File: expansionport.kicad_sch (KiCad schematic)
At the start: 18 parts, among them J20 C64_Expansion_Port, U31 74LS04, U32 74LVC374, U33 74LVC374, U34 74LVC374, U35 74LS374, U36 74LS374, U37 74LS374, U38 74LVC374, U39 74LVC374, U40 74LS374, U41 74LS374, U42 74LS06

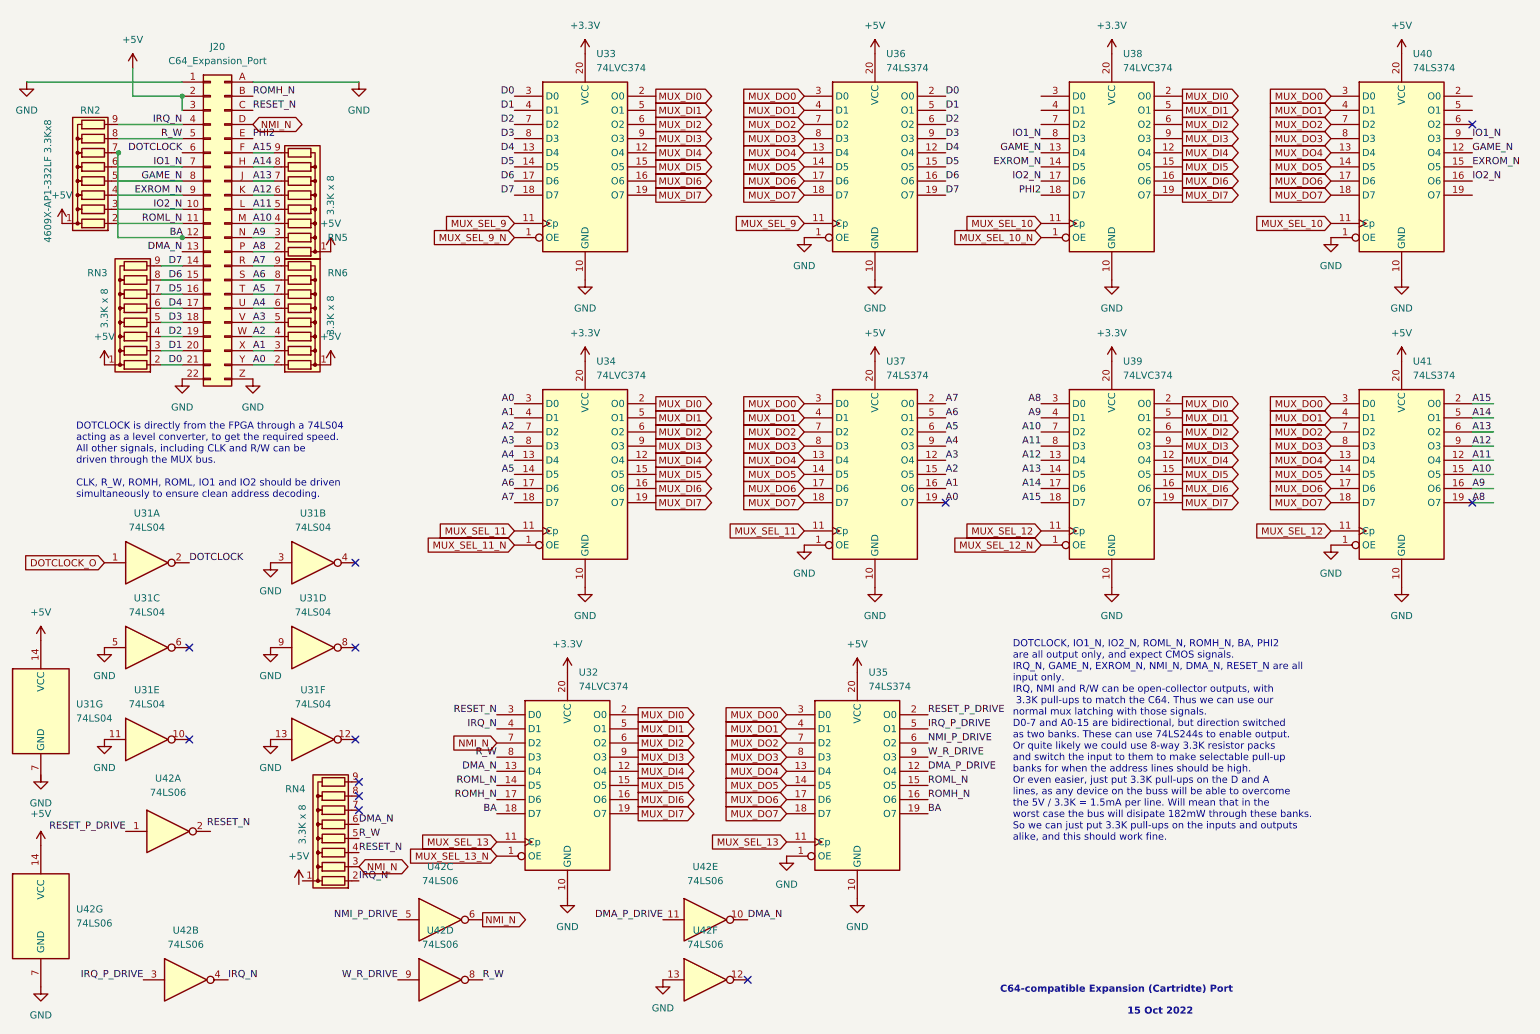
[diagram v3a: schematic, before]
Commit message: route part of cart port
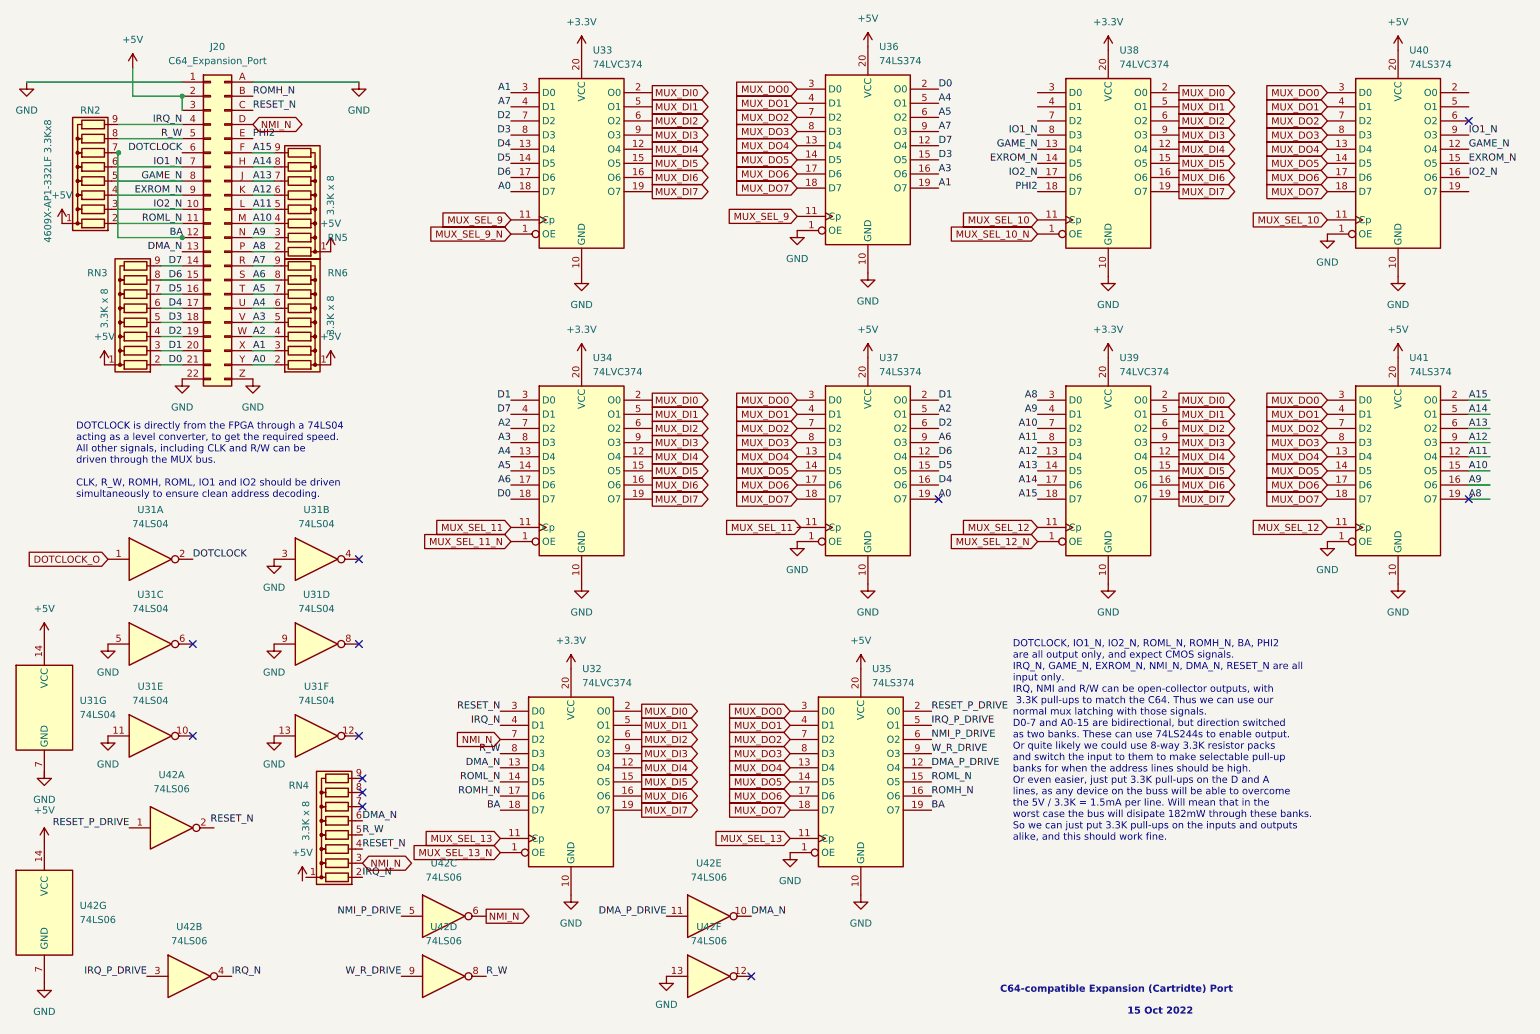
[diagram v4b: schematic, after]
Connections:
- net A0: now also U33.18 (D7); no longer U34.3 (D0)
- net A1: now also U33.3 (D0), U36.19 (O7); no longer U34.4 (D1), U37.16 (O6)
- net A2: now also U37.5 (O1); no longer U37.15 (O5)
- net A3: now also U36.16 (O6); no longer U37.12 (O4)
- net A4: now also U36.5 (O1); no longer U37.9 (O3)
- net A5: now also U36.6 (O2); no longer U37.6 (O2)
- net A6: now also U37.9 (O3); no longer U37.5 (O1)
- net A7: now also U33.4 (D1), U36.9 (O3); no longer U34.18 (D7), U37.2 (O0)
- net D0: now also U34.18 (D7); no longer U33.3 (D0)
- net D1: now also U34.3 (D0), U37.2 (O0); no longer U33.4 (D1), U36.5 (O1)
- net D2: now also U37.6 (O2); no longer U36.6 (O2)
- net D3: now also U36.15 (O5); no longer U36.9 (O3)
- net D4: now also U37.16 (O6); no longer U36.12 (O4)
- net D5: now also U37.15 (O5); no longer U36.15 (O5)
- net D6: now also U37.12 (O4); no longer U36.16 (O6)
- net D7: now also U34.4 (D1), U36.12 (O4); no longer U33.18 (D7), U36.19 (O7)
- net MUX_SEL_11: no longer U37.11 (Cp)
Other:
- moved on the sheet: RN4, U31A, U31B, U31C, U31D, U31E, U31F, U31G, U32, U33, U34, U35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

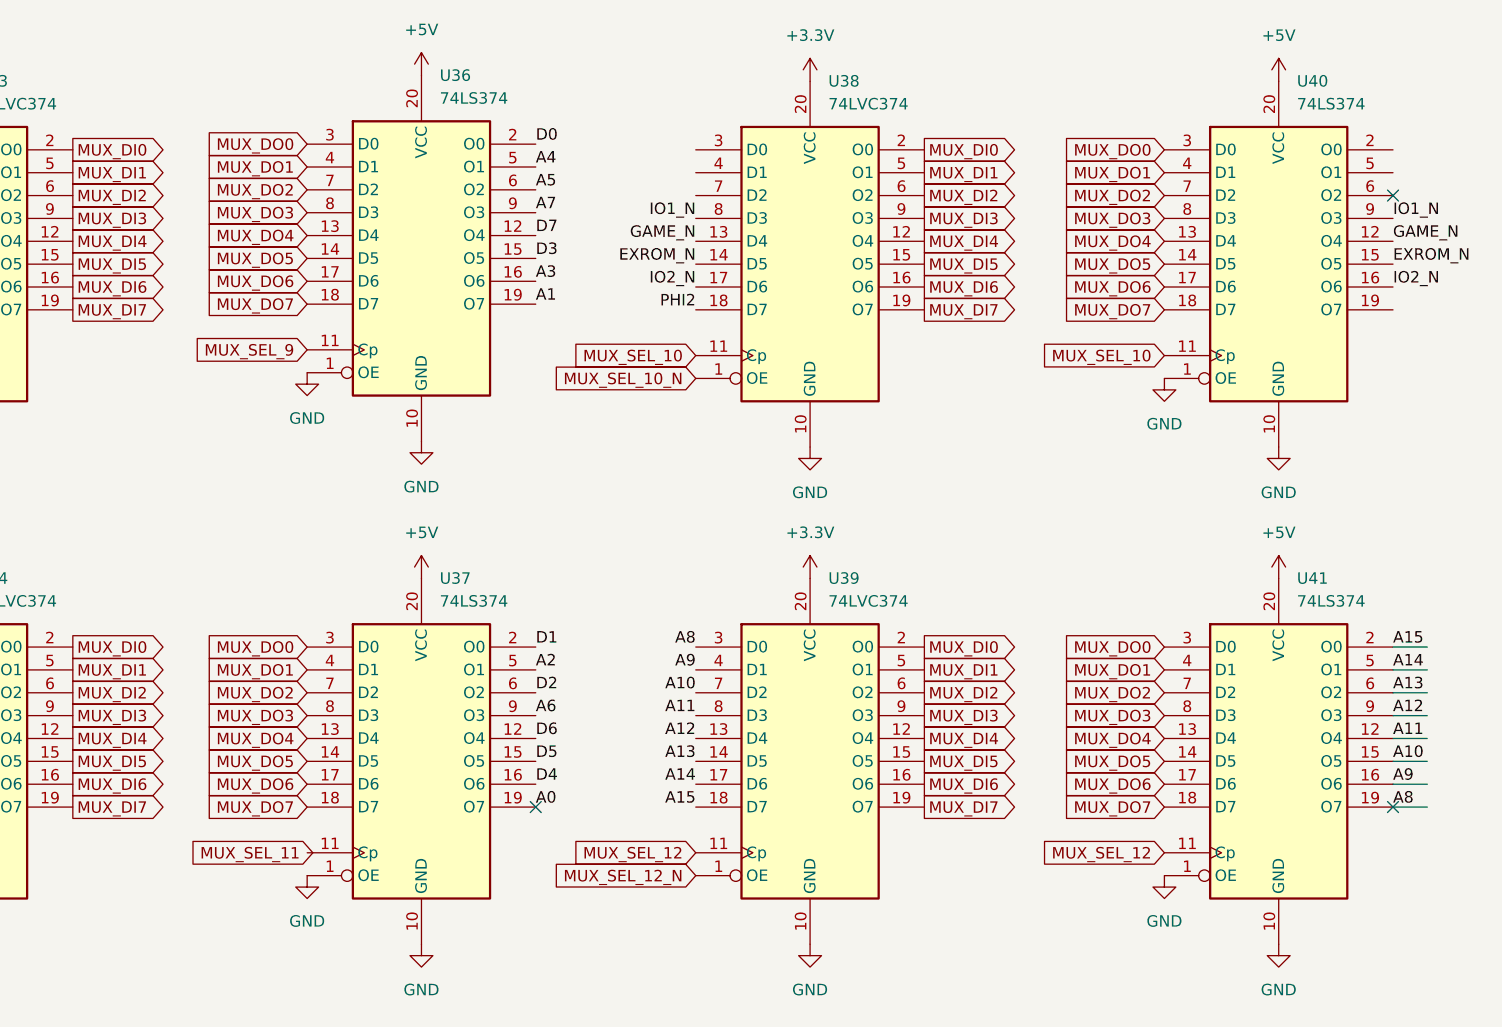
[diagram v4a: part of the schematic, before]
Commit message: begin routing mux bus
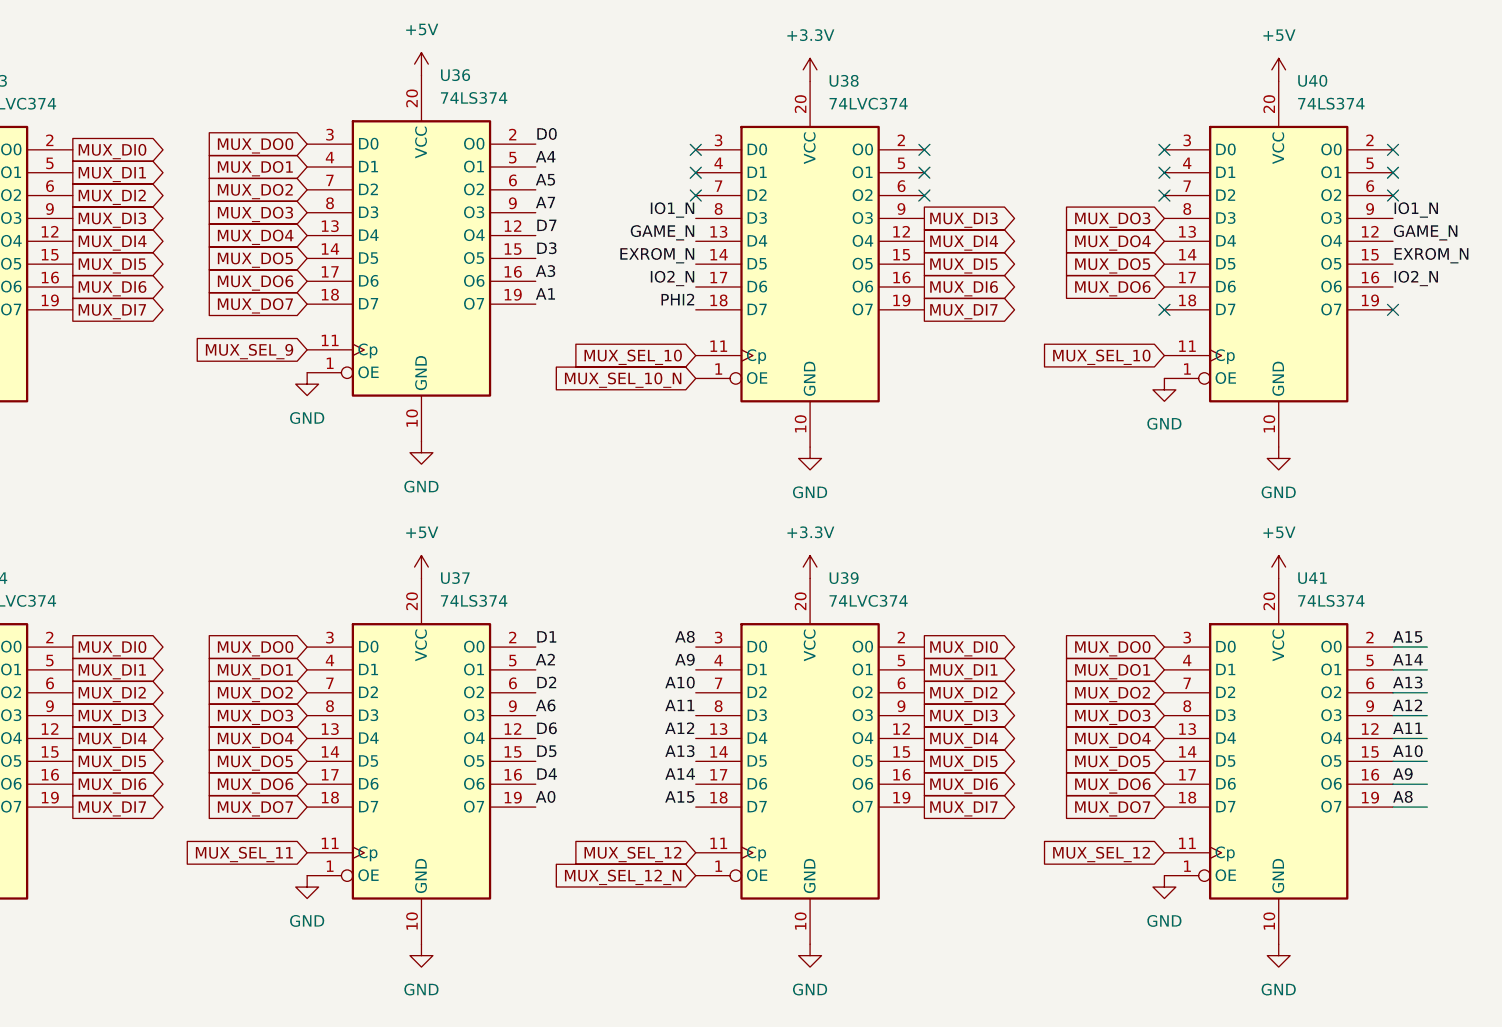
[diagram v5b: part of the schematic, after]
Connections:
- net MUX_DI0: no longer U38.2 (O0)
- net MUX_DI1: no longer U38.5 (O1)
- net MUX_DI2: no longer U38.6 (O2)
- net MUX_DO0: no longer U40.3 (D0)
- net MUX_DO1: no longer U40.4 (D1)
- net MUX_DO2: no longer U40.7 (D2)
- net MUX_DO7: no longer U40.18 (D7)
- net MUX_SEL_11: now also U37.11 (Cp)
- no-connect marks 12 -> 23
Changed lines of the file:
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@@
   (junction (at 44.45 29.21) (diameter 0) (color 0 0 0 0)
   )
-  (no_connect (at 180.34 101.6))
   (no_connect (at 76.835 154.305))
   (no_connect (at 76.2 127.635))
   (no_connect (at 275.59 33.655))
+  (no_connect (at 250.19 33.655))
   (no_connect (at 76.835 151.765))
+  (no_connect (at 275.59 31.115))
   (no_connect (at 76.2 112.395))
+  (no_connect (at 223.52 31.115))
   (no_connect (at 76.2 144.145))
+  (no_connect (at 275.59 46.355))
+  (no_connect (at 275.59 28.575))
+  (no_connect (at 223.52 28.575))
   (no_connect (at 46.355 127.635))
+  (no_connect (at 250.19 28.575))
+  (no_connect (at 198.12 33.655))
   (no_connect (at 146.685 187.325))
   (no_connect (at 76.835 156.845))
-  (no_connect (at 275.59 101.6))
+  (no_connect (at 250.19 31.115))
+  (no_connect (at 250.19 46.355))
+  (no_connect (at 198.12 31.115))
+  (no_connect (at 198.12 28.575))
   (no_connect (at 46.355 144.145))
+  (no_connect (at 223.52 33.655))
   (wire (pts (xy 40.64 59.69) (xy 44.45 59.69))
     (stroke (width 0) (type default) (color 0 0 0 0))
@@
     )
   )
-  (global_label "MUX_DO2" (shape input) (at 250.19 33.655 180) (fields_autoplaced)
-    (effects (font (size 1.27 1.27)) (justify right))
-    (property "Intersheet References" "${INTERSHEET_REFS}" (id 0) (at 239.0079 33.5756 0)
-      (effects (font (size 1.27 1.27)) (justify right) hide)
-    )
-  )
   (global_label "MUX_SEL_12" (shape input) (at 198.12 106.68 180) (fields_autoplaced)
     (effects (font (size 1.27 1.27)) (justify right))
@@
     )
   )
-  (global_label "MUX_SEL_11" (shape input) (at 155.575 106.68 180) (fields_autoplaced)
-    (effects (font (size 1.27 1.27)) (justify right))
-    (property "Intersheet References" "${INTERSHEET_REFS}" (id 0) (at 141.4295 106.6006 0)
-      (effects (font (size 1.27 1.27)) (justify right) hide)
-    )
-  )
-  (global_label "MUX_DI1" (shape output) (at 223.52 31.115 0) (fields_autoplaced)
-    (effects (font (size 1.27 1.27)) (justify left))
-    (property "Intersheet References" "${INTERSHEET_REFS}" (id 0) (at 233.9764 31.0356 0)
-      (effects (font (size 1.27 1.27)) (justify left) hide)
+  (global_label "MUX_SEL_11" (shape input) (at 154.94 106.68 180) (fields_autoplaced)
+    (effects (font (size 1.27 1.27)) (justify right))
+    (property "Intersheet References" "${INTERSHEET_REFS}" (id 0) (at 140.7945 106.6006 0)
+      (effects (font (size 1.27 1.27)) (justify right) hide)
     )
   )
@@
     )
   )
-  (global_label "MUX_DI0" (shape output) (at 223.52 28.575 0) (fields_autoplaced)
-    (effects (font (size 1.27 1.27)) (justify left))
-    (property "Intersheet References" "${INTERSHEET_REFS}" (id 0) (at 233.9764 28.4956 0)
-      (effects (font (size 1.27 1.27)) (justify left) hide)
-    )
-  )
   (global_label "MUX_DO2" (shape input) (at 250.19 88.9 180) (fields_autoplaced)
     (effects (font (size 1.27 1.27)) (justify right))
@@
     )
   )
-  (global_label "MUX_DO0" (shape input) (at 250.19 28.575 180) (fields_autoplaced)
-    (effects (font (size 1.27 1.27)) (justify right))
-    (property "Intersheet References" "${INTERSHEET_REFS}" (id 0) (at 239.0079 28.4956 0)
-      (effects (font (size 1.27 1.27)) (justify right) hide)
-    )
-  )
   (global_label "MUX_DI2" (shape output) (at 128.905 33.655 0) (fields_autoplaced)
     (effects (font (size 1.27 1.27)) (justify left))
@@
     )
   )
-  (global_label "MUX_DO1" (shape input) (at 250.19 31.115 180) (fields_autoplaced)
-    (effects (font (size 1.27 1.27)) (justify right))
-    (property "Intersheet References" "${INTERSHEET_REFS}" (id 0) (at 239.0079 31.0356 0)
-      (effects (font (size 1.27 1.27)) (justify right) hide)
-    )
-  )
   (global_label "MUX_DI6" (shape output) (at 128.905 99.06 0) (fields_autoplaced)
     (effects (font (size 1.27 1.27)) (justify left))
@@
     )
   )
-  (global_label "MUX_DI2" (shape output) (at 223.52 33.655 0) (fields_autoplaced)
-    (effects (font (size 1.27 1.27)) (justify left))
-    (property "Intersheet References" "${INTERSHEET_REFS}" (id 0) (at 233.9764 33.5756 0)
-      (effects (font (size 1.27 1.27)) (justify left) hide)
-    )
-  )
   (global_label "MUX_DI5" (shape output) (at 127 152.4 0) (fields_autoplaced)
     (effects (font (size 1.27 1.27)) (justify left))
@@
       (effects (font (size 1.27 1.27)) (justify right) hide)
     )
-  )
-  (global_label "MUX_DO7" (shape input) (at 250.19 46.355 180) (fields_autoplaced)
-    (effects (font (size 1.27 1.27)) (justify right))
-    (property "Intersheet References" "${INTERSHEET_REFS}" (id 0) (at 239.0079 46.2756 0)
-      (effects (font (size 1.27 1.27)) (justify right) hide)
-    )
